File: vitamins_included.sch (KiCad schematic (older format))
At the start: 6 parts

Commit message: Added BOM and 3D file
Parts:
- FID1, FID2, FID3, FID4, FID5, FID6: symbol lets_split_panel-rescue:Fiducial-RESCUE-lets_split_panel -> vitamins_included-rescue:Fiducial-RESCUE-lets_split_panel-lets_split_panel-rescue
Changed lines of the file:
@@
 EESchema Schematic File Version 4
-LIBS:lets_split_panel-cache
+LIBS:vitamins_included-cache
 EELAYER 26 0
 EELAYER END
@@
 $EndSheet
 $Comp
-L lets_split_panel-rescue:Fiducial-RESCUE-lets_split_panel FID1
+L vitamins_included-rescue:Fiducial-RESCUE-lets_split_panel-lets_split_panel-rescue FID1
 U 1 1 5A2A708E
 P 3725 5125
@@
 $EndComp
 $Comp
-L lets_split_panel-rescue:Fiducial-RESCUE-lets_split_panel FID2
+L vitamins_included-rescue:Fiducial-RESCUE-lets_split_panel-lets_split_panel-rescue FID2
 U 1 1 5A2A7142
 P 4700 5125
@@
 $EndComp
 $Comp
-L lets_split_panel-rescue:Fiducial-RESCUE-lets_split_panel FID3
+L vitamins_included-rescue:Fiducial-RESCUE-lets_split_panel-lets_split_panel-rescue FID3
 U 1 1 5A2A71BE
 P 6825 5075
@@
 $EndComp
 $Comp
-L lets_split_panel-rescue:Fiducial-RESCUE-lets_split_panel FID4
+L vitamins_included-rescue:Fiducial-RESCUE-lets_split_panel-lets_split_panel-rescue FID4
 U 1 1 5A2A7248
 P 7800 5075
@@
 $EndComp
 $Comp
-L lets_split_panel-rescue:Fiducial-RESCUE-lets_split_panel FID5
+L vitamins_included-rescue:Fiducial-RESCUE-lets_split_panel-lets_split_panel-rescue FID5
 U 1 1 5A2A77D2
 P 3725 5525
@@
 $EndComp
 $Comp
-L lets_split_panel-rescue:Fiducial-RESCUE-lets_split_panel FID6
+L vitamins_included-rescue:Fiducial-RESCUE-lets_split_panel-lets_split_panel-rescue FID6
 U 1 1 5A2A7850
 P 6825 5525

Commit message: Broke something. who knows
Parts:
- added Q?: Q_NMOS_GDS, symbol Device:Q_NMOS_GDS
- added Q?: Q_PMOS_GDS, symbol Device:Q_PMOS_GDS
- added R? (x2): 10k, symbol Device:R_Small
- added R?: LOAD, symbol Device:R
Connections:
- net labels added: GND
- wire segments 0 -> 15
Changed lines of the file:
@@
 	1    0    0    -1
 $EndComp
+$Comp
+L Device:Q_NMOS_GDS Q?
+U 1 1 5B78818D
+P 19625 2125
+F 0 "Q?" H 19830 2171 50  0000 L CNN
+F 1 "Q_NMOS_GDS" H 19100 2225 50  0000 L CNN
+F 2 "" H 19825 2225 50  0001 C CNN
+F 3 "~" H 19625 2125 50  0001 C CNN
+	1    19625 2125
+	1    0    0    -1
+$EndComp
+$Comp
+L Device:Q_PMOS_GDS Q?
+U 1 1 5B7881F9
+P 20000 1850
+F 0 "Q?" H 20206 1804 50  0000 L CNN
+F 1 "Q_PMOS_GDS" H 20225 1700 50  0000 L CNN
+F 2 "" H 20200 1950 50  0001 C CNN
+F 3 "~" H 20000 1850 50  0001 C CNN
+	1    20000 1850
+	1    0    0    1
+$EndComp
+Wire Wire Line
+	19800 1850 19725 1850
+Wire Wire Line
+	19725 1850 19725 1925
+$Comp
+L Device:R_Small R?
+U 1 1 5B788596
+P 19725 1700
+F 0 "R?" H 19666 1654 50  0000 R CNN
+F 1 "10k" H 19666 1745 50  0000 R CNN
+F 2 "" H 19725 1700 50  0001 C CNN
+F 3 "~" H 19725 1700 50  0001 C CNN
+	1    19725 1700
+	1    0    0    1
+$EndComp
+Wire Wire Line
+	19725 1800 19725 1850
+Connection ~ 19725 1850
+Wire Wire Line
+	19725 1600 19725 1550
+Wire Wire Line
+	19725 1550 20100 1550
+Wire Wire Line
+	20100 1550 20100 1650
+Wire Wire Line
+	20100 1550 20100 1500
+Connection ~ 20100 1550
+$Comp
+L Device:R_Small R?
+U 1 1 5B7886E2
+P 19375 2275
+F 0 "R?" H 19316 2229 50  0000 R CNN
+F 1 "10k" H 19316 2320 50  0000 R CNN
+F 2 "" H 19375 2275 50  0001 C CNN
+F 3 "~" H 19375 2275 50  0001 C CNN
+	1    19375 2275
+	1    0    0    1
+$EndComp
+Wire Wire Line
+	19425 2125 19375 2125
+Wire Wire Line
+	19375 2125 19375 2175
+Wire Wire Line
+	19375 2375 19375 2425
+Wire Wire Line
+	19375 2425 19725 2425
+Wire Wire Line
+	19725 2425 19725 2325
+$Comp
+L Device:R R?
+U 1 1 5B7888A8
+P 20100 2200
+F 0 "R?" H 20170 2246 50  0000 L CNN
+F 1 "LOAD" H 20170 2155 50  0000 L CNN
+F 2 "" V 20030 2200 50  0001 C CNN
+F 3 "~" H 20100 2200 50  0001 C CNN
+	1    20100 2200
+	1    0    0    -1
+$EndComp
+$Comp
+L power:GND #PWR?
+U 1 1 5B788958
+P 20100 2475
+F 0 "#PWR?" H 20100 2225 50  0001 C CNN
+F 1 "GND" H 20105 2302 50  0000 C CNN
+F 2 "" H 20100 2475 50  0001 C CNN
+F 3 "" H 20100 2475 50  0001 C CNN
+	1    20100 2475
+	1    0    0    -1
+$EndComp
+Wire Wire Line
+	20100 2475 20100 2425
+Wire Wire Line
+	20100 2425 19725 2425
+Connection ~ 19725 2425
+Wire Wire Line
+	20100 2350 20100 2425
+Connection ~ 20100 2425
 $EndSCHEMATC

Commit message: Added WS2812B leds to one half
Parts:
- removed Q?: Q_NMOS_GDS, symbol Device:Q_NMOS_GDS
- removed Q?: Q_PMOS_GDS, symbol Device:Q_PMOS_GDS
- removed R? (x2): 10k, symbol Device:R_Small
- removed R?: LOAD, symbol Device:R
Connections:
- net labels removed: GND
- wire segments 15 -> 0
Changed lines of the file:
@@
 	1    0    0    -1
 $EndComp
-$Comp
-L Device:Q_NMOS_GDS Q?
-U 1 1 5B78818D
-P 19625 2125
-F 0 "Q?" H 19830 2171 50  0000 L CNN
-F 1 "Q_NMOS_GDS" H 19100 2225 50  0000 L CNN
-F 2 "" H 19825 2225 50  0001 C CNN
-F 3 "~" H 19625 2125 50  0001 C CNN
-	1    19625 2125
-	1    0    0    -1
-$EndComp
-$Comp
-L Device:Q_PMOS_GDS Q?
-U 1 1 5B7881F9
-P 20000 1850
-F 0 "Q?" H 20206 1804 50  0000 L CNN
-F 1 "Q_PMOS_GDS" H 20225 1700 50  0000 L CNN
-F 2 "" H 20200 1950 50  0001 C CNN
-F 3 "~" H 20000 1850 50  0001 C CNN
-	1    20000 1850
-	1    0    0    1
-$EndComp
-Wire Wire Line
-	19800 1850 19725 1850
-Wire Wire Line
-	19725 1850 19725 1925
-$Comp
-L Device:R_Small R?
-U 1 1 5B788596
-P 19725 1700
-F 0 "R?" H 19666 1654 50  0000 R CNN
-F 1 "10k" H 19666 1745 50  0000 R CNN
-F 2 "" H 19725 1700 50  0001 C CNN
-F 3 "~" H 19725 1700 50  0001 C CNN
-	1    19725 1700
-	1    0    0    1
-$EndComp
-Wire Wire Line
-	19725 1800 19725 1850
-Connection ~ 19725 1850
-Wire Wire Line
-	19725 1600 19725 1550
-Wire Wire Line
-	19725 1550 20100 1550
-Wire Wire Line
-	20100 1550 20100 1650
-Wire Wire Line
-	20100 1550 20100 1500
-Connection ~ 20100 1550
-$Comp
-L Device:R_Small R?
-U 1 1 5B7886E2
-P 19375 2275
-F 0 "R?" H 19316 2229 50  0000 R CNN
-F 1 "10k" H 19316 2320 50  0000 R CNN
-F 2 "" H 19375 2275 50  0001 C CNN
-F 3 "~" H 19375 2275 50  0001 C CNN
-	1    19375 2275
-	1    0    0    1
-$EndComp
-Wire Wire Line
-	19425 2125 19375 2125
-Wire Wire Line
-	19375 2125 19375 2175
-Wire Wire Line
-	19375 2375 19375 2425
-Wire Wire Line
-	19375 2425 19725 2425
-Wire Wire Line
-	19725 2425 19725 2325
-$Comp
-L Device:R R?
-U 1 1 5B7888A8
-P 20100 2200
-F 0 "R?" H 20170 2246 50  0000 L CNN
-F 1 "LOAD" H 20170 2155 50  0000 L CNN
-F 2 "" V 20030 2200 50  0001 C CNN
-F 3 "~" H 20100 2200 50  0001 C CNN
-	1    20100 2200
-	1    0    0    -1
-$EndComp
-$Comp
-L power:GND #PWR?
-U 1 1 5B788958
-P 20100 2475
-F 0 "#PWR?" H 20100 2225 50  0001 C CNN
-F 1 "GND" H 20105 2302 50  0000 C CNN
-F 2 "" H 20100 2475 50  0001 C CNN
-F 3 "" H 20100 2475 50  0001 C CNN
-	1    20100 2475
-	1    0    0    -1
-$EndComp
-Wire Wire Line
-	20100 2475 20100 2425
-Wire Wire Line
-	20100 2425 19725 2425
-Connection ~ 19725 2425
-Wire Wire Line
-	20100 2350 20100 2425
-Connection ~ 20100 2425
 $EndSCHEMATC

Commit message: Fixed symbols to not rely on rescue
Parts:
- FID1, FID2, FID3, FID4, FID5, FID6: symbol vitamins_included-rescue:Fiducial-RESCUE-lets_split_panel-lets_split_panel-rescue -> Mechanical:Fiducial
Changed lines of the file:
@@
 $EndSheet
 $Comp
-L vitamins_included-rescue:Fiducial-RESCUE-lets_split_panel-lets_split_panel-rescue FID1
-U 1 1 5A2A708E
-P 3725 5125
-F 0 "FID1" H 3853 5178 60  0000 L CNN
-F 1 "Fiducial" H 3853 5072 60  0000 L CNN
-F 2 "Fiducials:Fiducial_1mm_Dia_2mm_Outer" H 3725 5125 60  0001 C CNN
-F 3 "" H 3725 5125 60  0001 C CNN
-	1    3725 5125
-	1    0    0    -1
-$EndComp
-$Comp
-L vitamins_included-rescue:Fiducial-RESCUE-lets_split_panel-lets_split_panel-rescue FID2
+L Mechanical:Fiducial FID2
 U 1 1 5A2A7142
 P 4700 5125
@@
 $EndComp
 $Comp
-L vitamins_included-rescue:Fiducial-RESCUE-lets_split_panel-lets_split_panel-rescue FID3
+L Mechanical:Fiducial FID3
 U 1 1 5A2A71BE
 P 6825 5075
@@
 $EndComp
 $Comp
-L vitamins_included-rescue:Fiducial-RESCUE-lets_split_panel-lets_split_panel-rescue FID4
+L Mechanical:Fiducial FID4
 U 1 1 5A2A7248
 P 7800 5075
@@
 $EndComp
 $Comp
-L vitamins_included-rescue:Fiducial-RESCUE-lets_split_panel-lets_split_panel-rescue FID5
+L Mechanical:Fiducial FID5
 U 1 1 5A2A77D2
 P 3725 5525
@@
 $EndComp
 $Comp
-L vitamins_included-rescue:Fiducial-RESCUE-lets_split_panel-lets_split_panel-rescue FID6
+L Mechanical:Fiducial FID6
 U 1 1 5A2A7850
 P 6825 5525
@@
 	1    0    0    -1
 $EndComp
+$Comp
+L Mechanical:Fiducial FID1
+U 1 1 5A2A708E
+P 3725 5125
+F 0 "FID1" H 3853 5178 60  0000 L CNN
+F 1 "Fiducial" H 3853 5072 60  0000 L CNN
+F 2 "Fiducials:Fiducial_1mm_Dia_2mm_Outer" H 3725 5125 60  0001 C CNN
+F 3 "" H 3725 5125 60  0001 C CNN
+	1    3725 5125
+	1    0    0    -1
+$EndComp

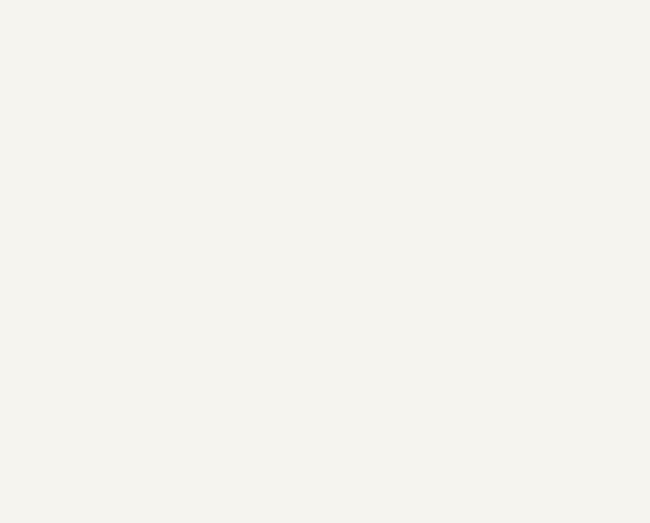
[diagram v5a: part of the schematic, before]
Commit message: Modified reset switch footprint for better manufacturing, and added updated gerbers
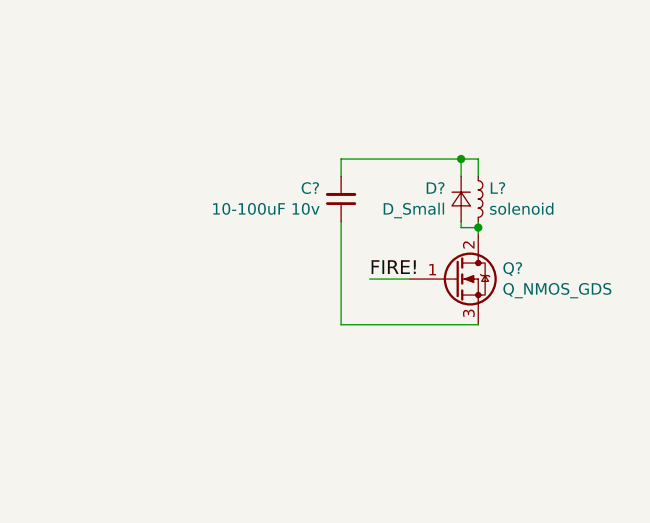
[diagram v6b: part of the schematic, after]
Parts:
- added C?: 10-100uF 10v, symbol Device:C_Small
- added D?: D_Small, symbol Device:D_Small
- added L?: solenoid, symbol Device:L_Small
- added Q?: Q_NMOS_GDS, symbol Device:Q_NMOS_GDS
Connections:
- new net: D?.2 (A), L?.2, Q?.2 (D)
- new net: C?.1, Q?.3 (S)
- new net: C?.2, D?.1 (K), L?.1
- new net FIRE!: Q?.1 (G)
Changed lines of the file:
@@
 	1    0    0    -1
 $EndComp
+$Comp
+L Device:Q_NMOS_GDS Q?
+U 1 1 5D766595
+P 16550 3350
+F 0 "Q?" H 16756 3396 50  0000 L CNN
+F 1 "Q_NMOS_GDS" H 16756 3305 50  0000 L CNN
+F 2 "" H 16750 3450 50  0001 C CNN
+F 3 "~" H 16550 3350 50  0001 C CNN
+	1    16550 3350
+	1    0    0    -1
+$EndComp
+$Comp
+L Device:L_Small L?
+U 1 1 5D768156
+P 16650 3000
+F 0 "L?" H 16698 3046 50  0000 L CNN
+F 1 "solenoid" H 16698 2955 50  0000 L CNN
+F 2 "" H 16650 3000 50  0001 C CNN
+F 3 "~" H 16650 3000 50  0001 C CNN
+	1    16650 3000
+	1    0    0    -1
+$EndComp
+$Comp
+L Device:C_Small C?
+U 1 1 5D769480
+P 16050 3000
+F 0 "C?" H 15958 2954 50  0000 R CNN
+F 1 "10-100uF 10v" H 15958 3045 50  0000 R CNN
+F 2 "" H 16050 3000 50  0001 C CNN
+F 3 "~" H 16050 3000 50  0001 C CNN
+	1    16050 3000
+	1    0    0    1
+$EndComp
+Wire Wire Line
+	16050 2900 16050 2825
+Wire Wire Line
+	16050 2825 16575 2825
+Wire Wire Line
+	16650 2825 16650 2900
+$Comp
+L Device:D_Small D?
+U 1 1 5D76D373
+P 16575 3000
+F 0 "D?" V 16529 3068 50  0000 L CNN
+F 1 "D_Small" V 16620 3068 50  0000 L CNN
+F 2 "" V 16575 3000 50  0001 C CNN
+F 3 "~" V 16575 3000 50  0001 C CNN
+	1    16575 3000
+	0    -1   1    0
+$EndComp
+Wire Wire Line
+	16350 3350 16175 3350
+Text Label 16175 3350 0    60   ~ 0
+FIRE!
+Wire Wire Line
+	16050 3100 16050 3550
+Wire Wire Line
+	16050 3550 16650 3550
+Wire Wire Line
+	16650 3100 16650 3125
+Wire Wire Line
+	16575 3100 16575 3125
+Wire Wire Line
+	16575 3125 16650 3125
+Connection ~ 16650 3125
+Wire Wire Line
+	16650 3125 16650 3150
+Wire Wire Line
+	16575 2900 16575 2825
+Connection ~ 16575 2825
+Wire Wire Line
+	16575 2825 16650 2825
 $EndSCHEMATC

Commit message: Added ESD protection to connectors
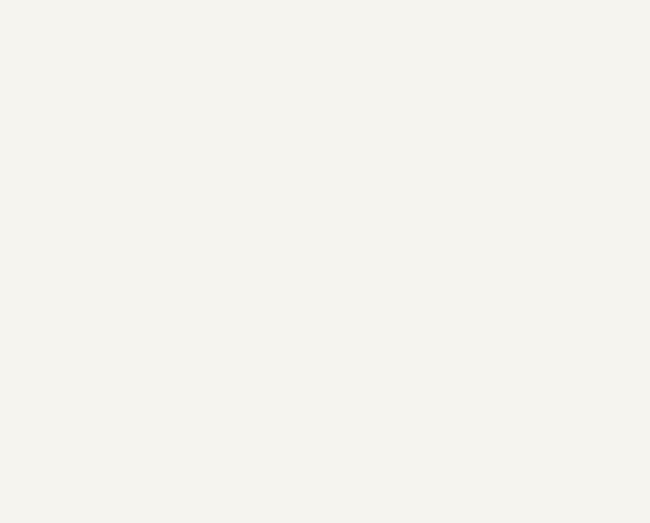
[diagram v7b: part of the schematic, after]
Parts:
- removed C?: 10-100uF 10v, symbol Device:C_Small
- removed D?: D_Small, symbol Device:D_Small
- removed L?: solenoid, symbol Device:L_Small
- removed Q?: Q_NMOS_GDS, symbol Device:Q_NMOS_GDS
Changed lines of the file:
@@
 	1    0    0    -1
 $EndComp
-$Comp
-L Device:Q_NMOS_GDS Q?
-U 1 1 5D766595
-P 16550 3350
-F 0 "Q?" H 16756 3396 50  0000 L CNN
-F 1 "Q_NMOS_GDS" H 16756 3305 50  0000 L CNN
-F 2 "" H 16750 3450 50  0001 C CNN
-F 3 "~" H 16550 3350 50  0001 C CNN
-	1    16550 3350
-	1    0    0    -1
-$EndComp
-$Comp
-L Device:L_Small L?
-U 1 1 5D768156
-P 16650 3000
-F 0 "L?" H 16698 3046 50  0000 L CNN
-F 1 "solenoid" H 16698 2955 50  0000 L CNN
-F 2 "" H 16650 3000 50  0001 C CNN
-F 3 "~" H 16650 3000 50  0001 C CNN
-	1    16650 3000
-	1    0    0    -1
-$EndComp
-$Comp
-L Device:C_Small C?
-U 1 1 5D769480
-P 16050 3000
-F 0 "C?" H 15958 2954 50  0000 R CNN
-F 1 "10-100uF 10v" H 15958 3045 50  0000 R CNN
-F 2 "" H 16050 3000 50  0001 C CNN
-F 3 "~" H 16050 3000 50  0001 C CNN
-	1    16050 3000
-	1    0    0    1
-$EndComp
-Wire Wire Line
-	16050 2900 16050 2825
-Wire Wire Line
-	16050 2825 16575 2825
-Wire Wire Line
-	16650 2825 16650 2900
-$Comp
-L Device:D_Small D?
-U 1 1 5D76D373
-P 16575 3000
-F 0 "D?" V 16529 3068 50  0000 L CNN
-F 1 "D_Small" V 16620 3068 50  0000 L CNN
-F 2 "" V 16575 3000 50  0001 C CNN
-F 3 "~" V 16575 3000 50  0001 C CNN
-	1    16575 3000
-	0    -1   1    0
-$EndComp
-Wire Wire Line
-	16350 3350 16175 3350
-Text Label 16175 3350 0    60   ~ 0
-FIRE!
-Wire Wire Line
-	16050 3100 16050 3550
-Wire Wire Line
-	16050 3550 16650 3550
-Wire Wire Line
-	16650 3100 16650 3125
-Wire Wire Line
-	16575 3100 16575 3125
-Wire Wire Line
-	16575 3125 16650 3125
-Connection ~ 16650 3125
-Wire Wire Line
-	16650 3125 16650 3150
-Wire Wire Line
-	16575 2900 16575 2825
-Connection ~ 16575 2825
-Wire Wire Line
-	16575 2825 16650 2825
 $EndSCHEMATC
